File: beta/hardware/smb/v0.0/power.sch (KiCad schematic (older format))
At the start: 5 parts, among them U202 LM1117IMP-3.3

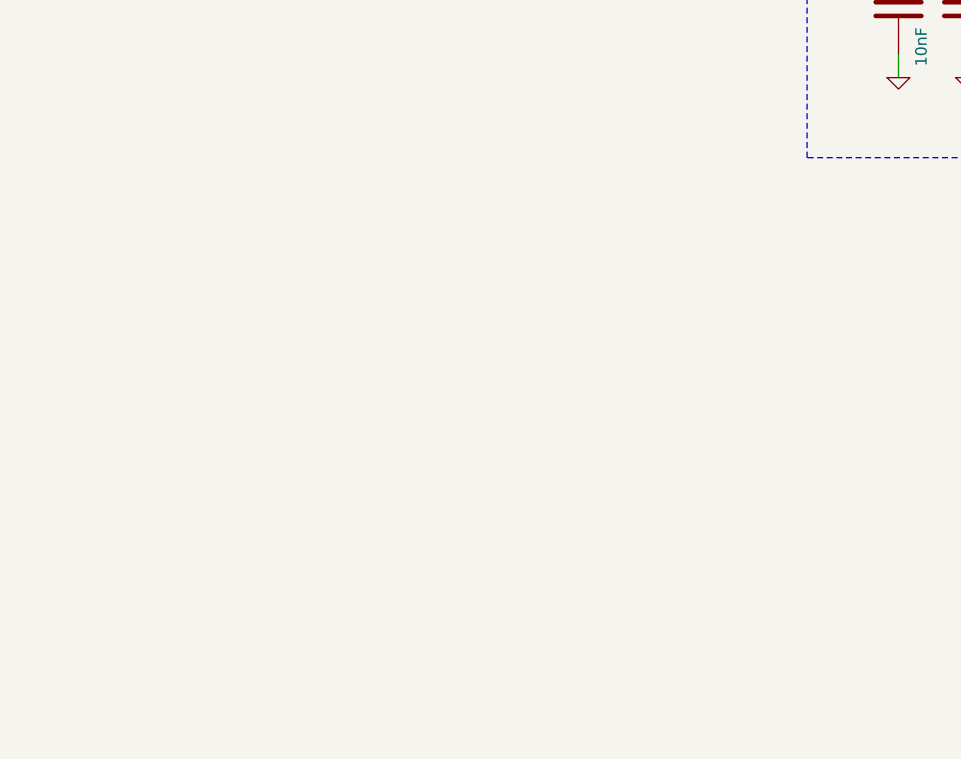
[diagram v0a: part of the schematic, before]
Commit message: Need to calculate value for mp2562 buck.
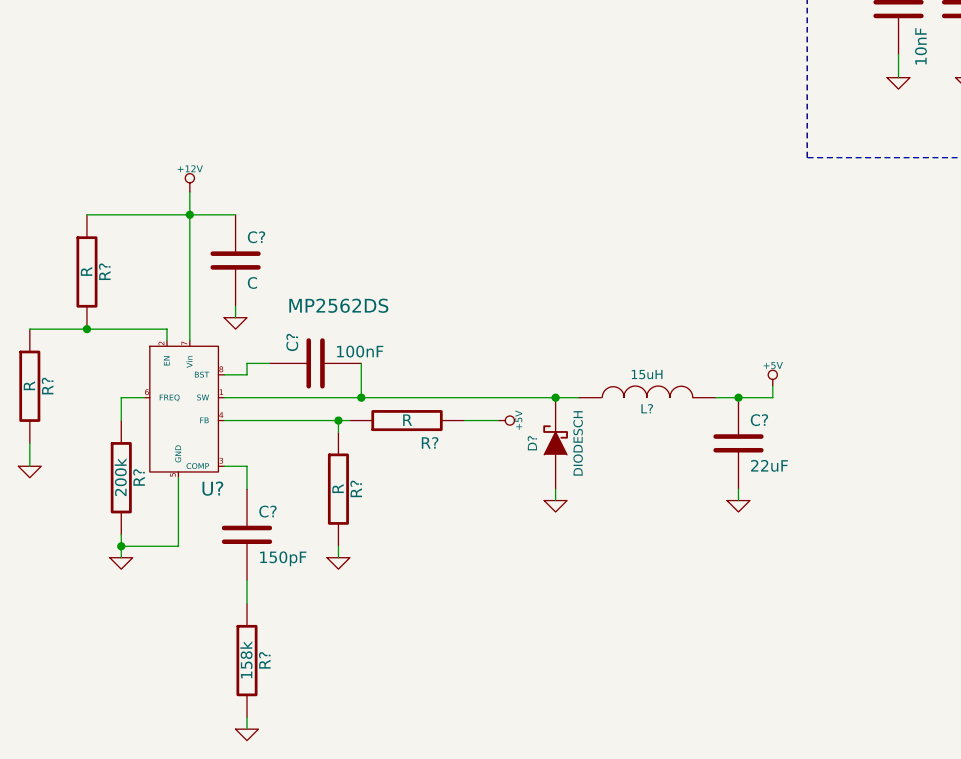
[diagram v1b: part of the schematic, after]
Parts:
- added C?: 100nF, symbol C
- added C?: 22uF, symbol C
- added C?: 150pF, symbol C
- added C?: C, symbol C
- added D?: DIODESCH, symbol DIODESCH
- added L?: 15uH, symbol INDUCTOR
- added R?: 200k, symbol R
- added R? (x4): R, symbol R
- added R?: 158k, symbol R
- added U?: MP2562DS, symbol MP2562DS
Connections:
- net +5V: now also C?.1, L?.2, R?.2
- net GND: now also C?.2, C?.2, D?.1 (A), R?.2, R?.2, R?.2, R?.2, U?.5 (GND)
- new net: C?.2, D?.2 (K), L?.1, U?.1 (SW)
- new net: R?.1, R?.2, U?.2 (EN)
- new net: C?.1, U?.3 (COMP)
- new net: R?.1, R?.1, U?.4 (FB)
- new net: R?.1, U?.6 (FREQ)
- new net: C?.1, U?.8 (BST)
- new net: C?.2, R?.1
- new net +12V: C?.1, R?.1, U?.7 (Vin)

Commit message: few modifications
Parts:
- removed C?: 100nF, symbol C
- removed C?: 22uF, symbol C
- removed C?: C, symbol C
- added C301, C303, C304, C310, C311: 1uF, symbol CSMALL
- added C305, C306, C307, C308, C312: 4.7uF, symbol CSMALL
- added C309: 100nF, symbol CSMALL
- R301: renamed from R?; value R -> 17.4k
- R302: renamed from R?; value R -> 100k
- R305: renamed from R?; value R -> 40.2k
- R306: renamed from R?; value R -> 210k
- gave numbers to parts that had none: 6
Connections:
- wire segments 40 -> 58

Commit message: New components and corrections
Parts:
- removed L301: 15uH, symbol INDUCTOR
- added L301: SRF1260-150M, symbol DUAL_IND
- added P301: CONN_2, symbol CONN_2
- C211, C212, C214, C302, C309, R301, R302, R303, R304, R305, R306: footprint (none) -> SM0603
- C213, C301, C303, C304, C305, C306, C307, C308, C310, C311, C312: footprint (none) -> SM0805
- D301: value DIODESCH -> B280-13-F
- U302: footprint (none) -> SO8E
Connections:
- wire segments 58 -> 64
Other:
- note added: "Self a cabler \nen mode parallele !!!"
